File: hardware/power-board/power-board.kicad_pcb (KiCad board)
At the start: 2 copper layers, 197 x 65 mm, 26 parts, among them J1 SW_SPST, J2 Main Board, J3 DMX512 Out Jack, J4 DMX512, K1 SPST-NO, K2 SPST-NO, P1 IEC320-C14, P2 IEC320-C13, P3 IEC320-C13, U1 NUD3112DMT1G, U2 MAX3075E

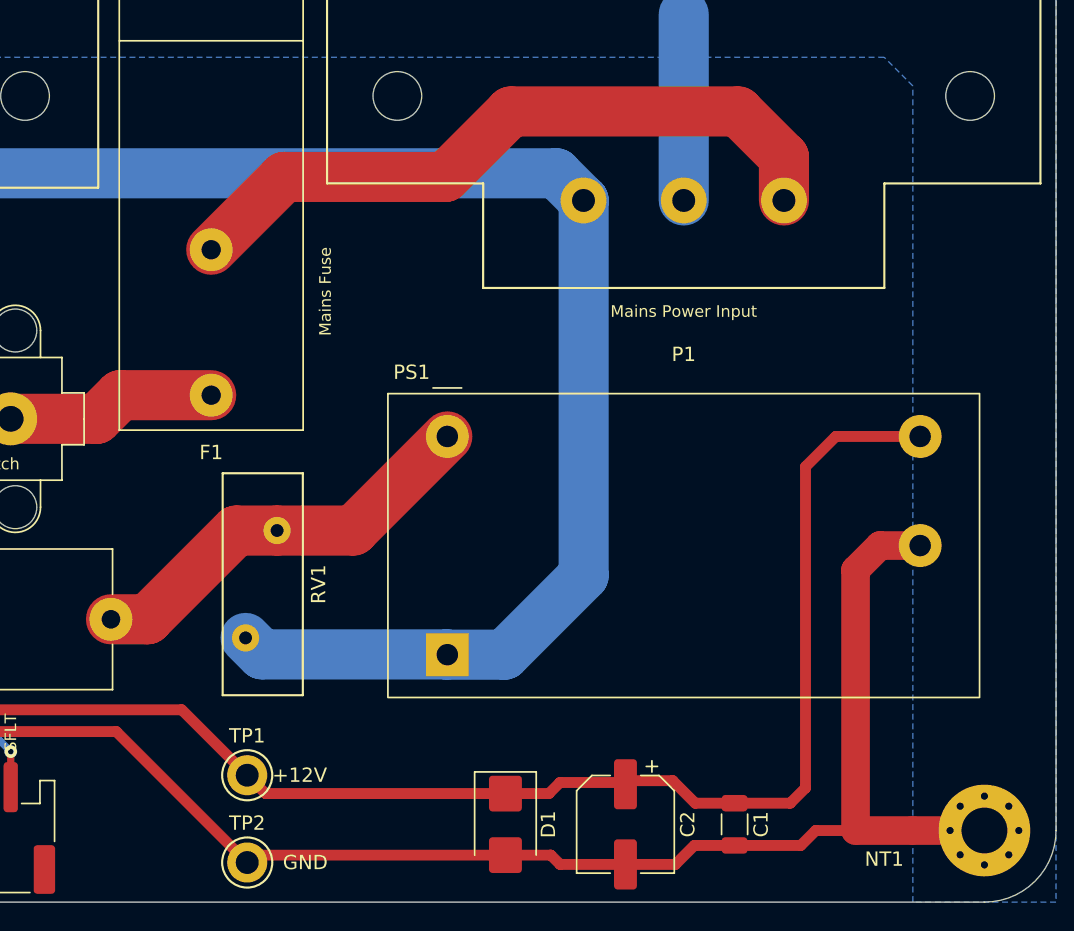
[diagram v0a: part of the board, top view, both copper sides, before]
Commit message: Swap AC/DC converter for IRM-10-12 and update output capacitor
A bit more comfortable with this option versus the other one, since it
likely has more protection and filtering.  Still may want to rearrange
and reroute some of the output components, which are a bit cramped at
the moment.
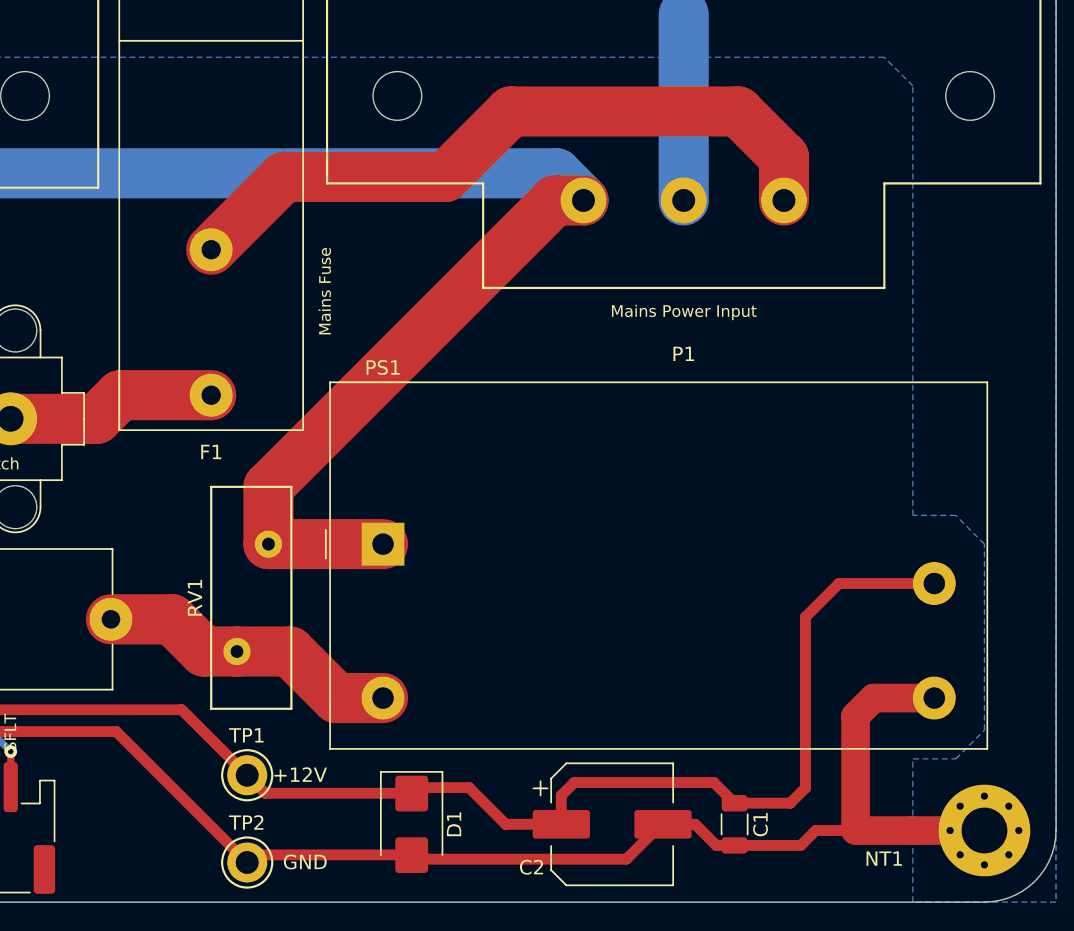
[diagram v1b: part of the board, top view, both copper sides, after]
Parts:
- C2: value 10uF -> 47uF; footprint Capacitor_SMD:CP_Elec_6.3x5.4 -> lib_fp:CP_Elec_8x10.2
- PS1: value CFM06S120-E -> IRM-10-12; footprint lib_fp:Converter_ACDC_Cincom_CFM06Sxxx-E -> Converter_ACDC:Converter_ACDC_MeanWell_IRM-10-xx_THT
- moved PS1 21.0 mm to (185.0, 80.0)
- moved RV1 6.74 mm to (177.0, 80.0), turned to -90 degrees
- moved D1 6.55 mm to (187.0, 99.6)
- moved C2 0.93 mm to (201.0, 99.6), turned to 0 degrees
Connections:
- PS1 pad 3: +12V -> GND
- PS1 pad 4: GND -> +12V
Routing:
- net NEUT: track 181.2 -> 170.9 mm
- net GND: track 117.0 -> 108.0 mm
- net /AC_L: track 28.8 -> 21.3 mm
- net +12V: track 191.6 -> 185.2 mm

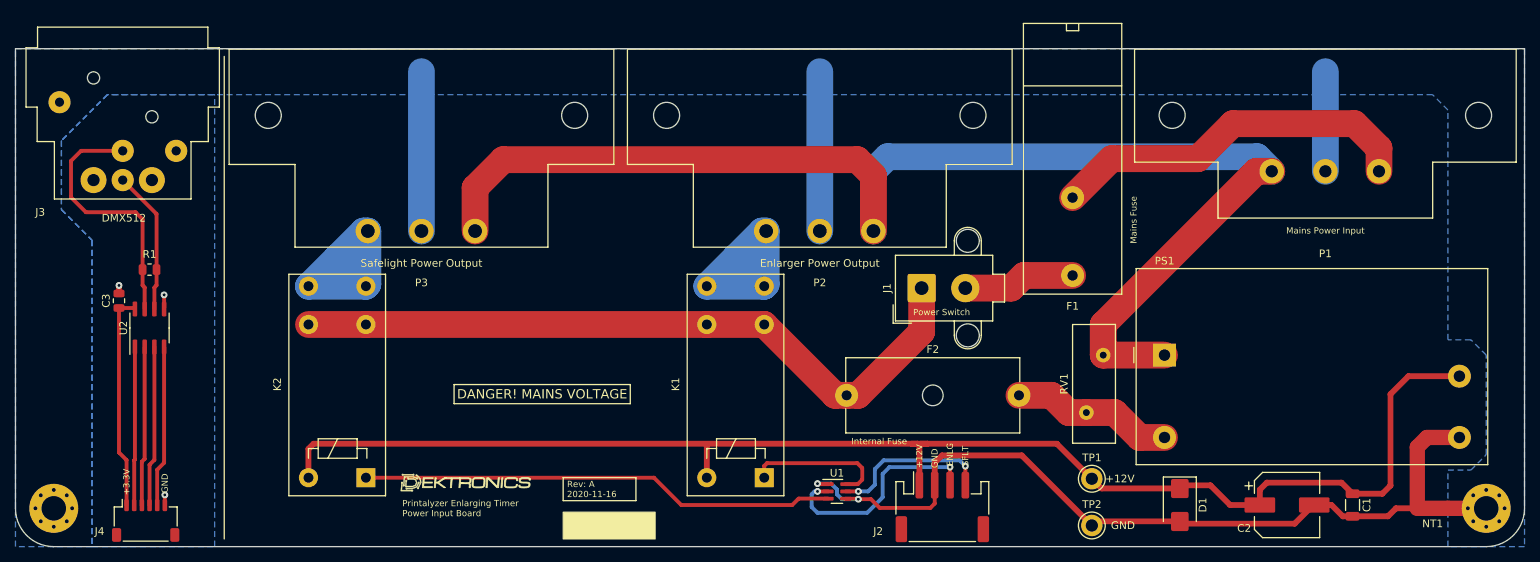
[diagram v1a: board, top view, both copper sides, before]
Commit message: Move components around for better clearance and update things
Moved the DC output filter components for better clearance
Moved one of the relays to make more space
Rerouted the relay control bits
Added a DC ground plane to make connections a bit better

Removed the net tie between DC ground and protective earth, as there's
still no good straight answer on how to do this. And they'll be
connected in other ways on the main board.
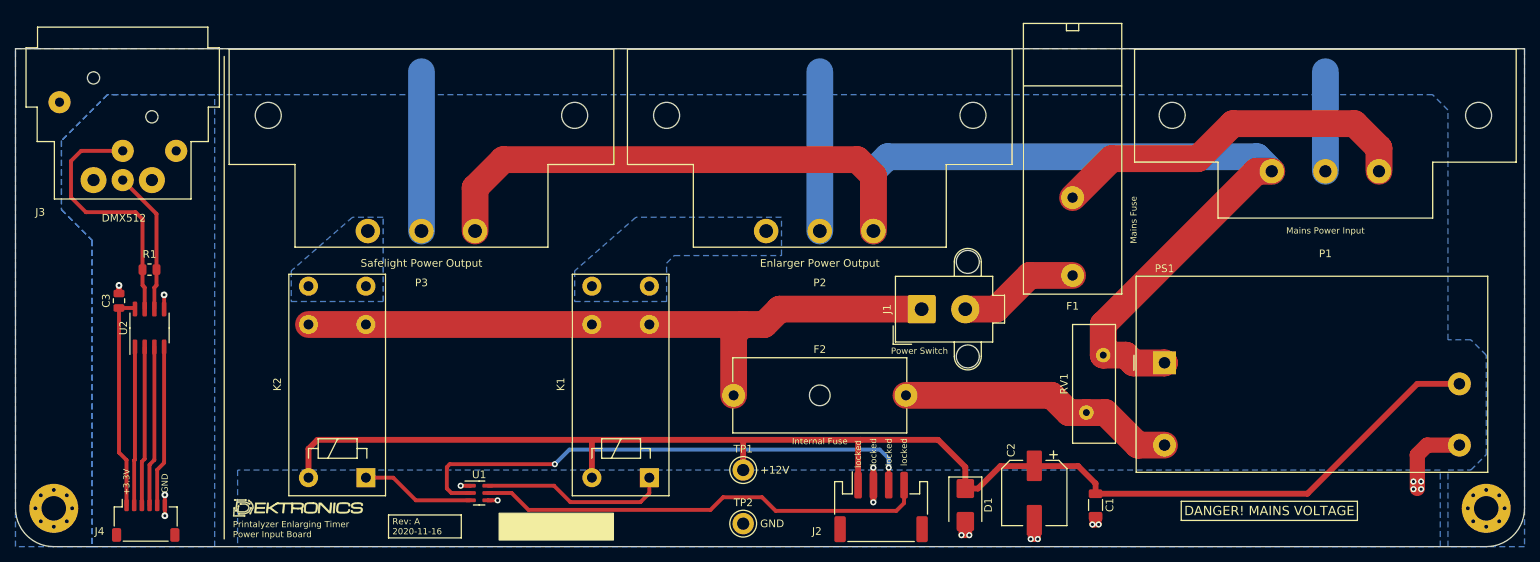
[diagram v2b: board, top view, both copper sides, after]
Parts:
- removed NT1: NetTie_2, NetTie:NetTie-2_SMD_Pad2.0mm
- moved U1 46.7 mm to (95.5, 98.0)
- moved TP1 45.5 mm to (130.0, 95.0)
- moved TP2 45.5 mm to (130.0, 102.0)
- moved C1 33.6 mm to (176.0, 99.6)
- moved C2 33.0 mm to (168.0, 98.0), turned to -90 degrees
- moved D1 28.0 mm to (159.0, 99.6)
- moved LOGO 22.1 mm to (72.1, 99.8)
- moved K1 15.0 mm to (110.2, 96.0)
- moved F2 14.8 mm to (128.8, 85.2)
- moved J2 8.00 mm to (148.0, 99.8)
- moved J1 2.75 mm to (153.3, 74.0)
- moved PS1 1.00 mm to (185.0, 81.0)
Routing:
- net GND: track 108.0 -> 37.8 mm, vias 2 -> 14
- net Net-(U1-DRAIN2): track 62.1 -> 14.9 mm
- net /RELAY_ENLARGER: track 28.9 -> 68.6 mm
- net /RELAY_SAFELIGHT: track 21.3 -> 59.4 mm, vias 2 -> 0
- net /ENLG_AC_L: track 30.9 -> 0.00 mm
- net /SFLT_AC_L: track 30.8 -> 0.00 mm
- net /AC_L: track 21.3 -> 36.4 mm
- net Net-(U1-DRAIN1): track 18.7 -> 24.5 mm
- net Earth: track 59.6 -> 54.6 mm
- net LINE: track 93.0 -> 90.6 mm
- net +12V: track 185.2 -> 183.2 mm
- net GND1: track 4.37 -> 5.74 mm, vias 3 -> 4
- net Net-(J1-B): track 14.7 -> 15.8 mm
- added copper zone on B.Cu, net /ENLG_AC_L
- added copper zone on B.Cu, net /SFLT_AC_L
- added copper zone on B.Cu, net GND
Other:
- board text added: "locked"
- board text removed: "ENLG"
- board text removed: "SFLT"

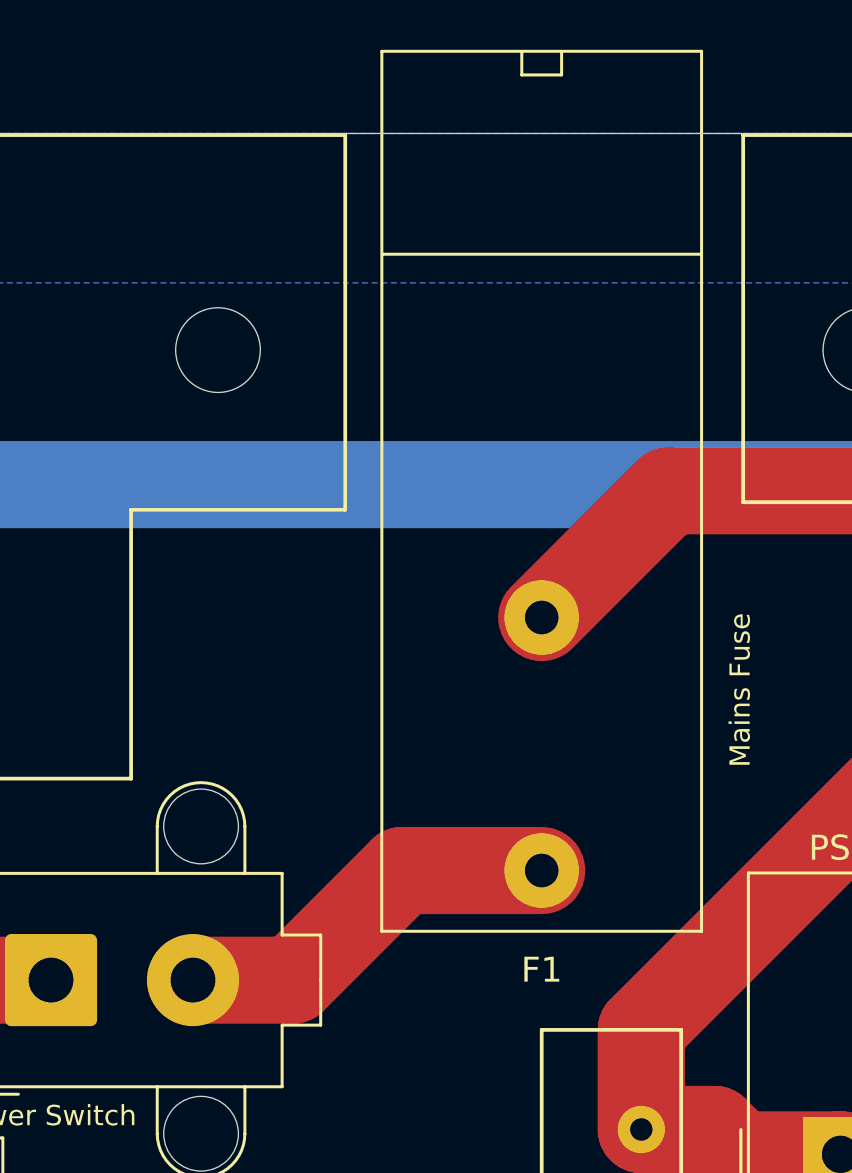
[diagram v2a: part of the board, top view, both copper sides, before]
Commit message: Changed fuse holder from Bulgin to Schurter
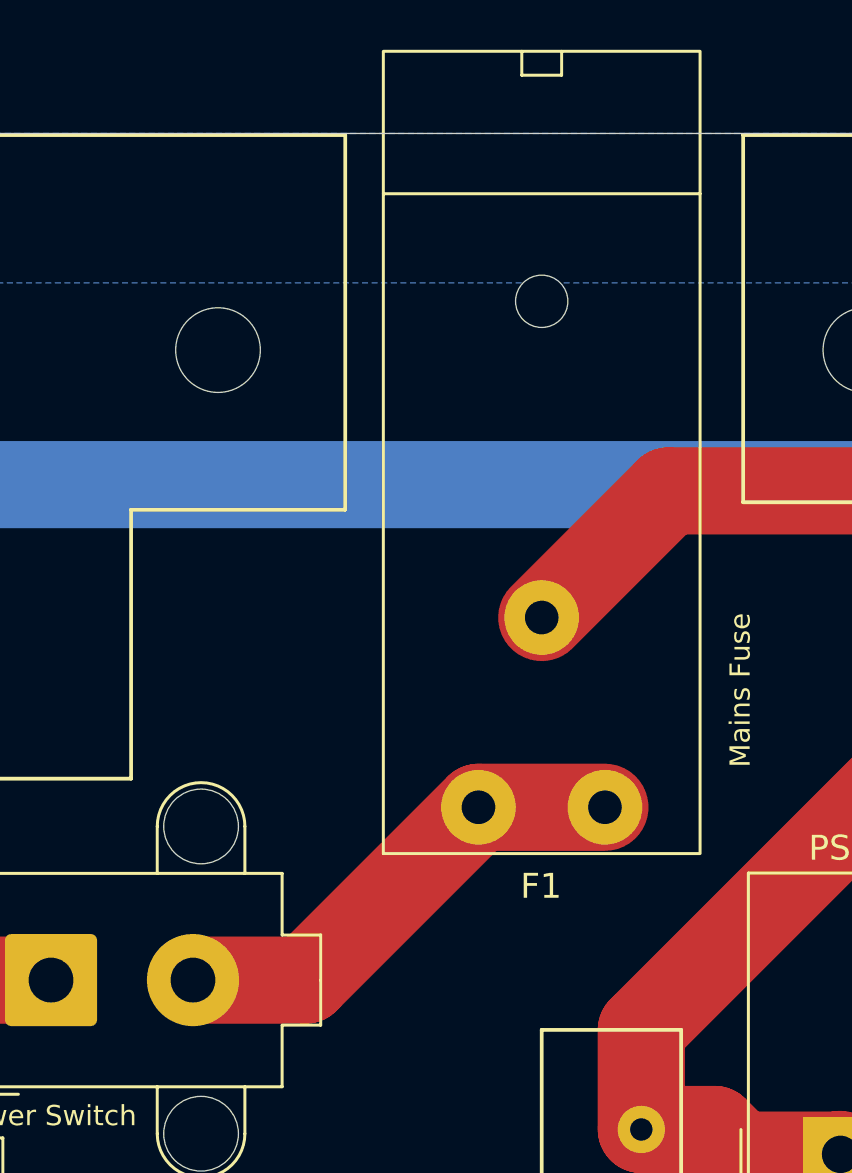
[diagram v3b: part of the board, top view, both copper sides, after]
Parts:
- F1: footprint Fuse:Fuseholder_Cylinder-5x20mm_Bulgin_FX0457_Horizontal_Closed -> lib_fp:Fuseholder_Cylinder-5x20mm_Schurter_FPG5_3101.0050_Horizontal_Closed
- moved F1 2.54 mm to (173.0, 67.1)
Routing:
- net Net-(J1-B): track 15.8 -> 19.4 mm
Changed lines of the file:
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@@
     )
   )
-  (footprint "Fuse:Fuseholder_Cylinder-5x20mm_Bulgin_FX0457_Horizontal_Closed" locked (layer "F.Cu")
-    (at 173 69.6 90)
-    (descr "Fuseholder, 5x20, closed, horizontal, Bulgin, FX0457, Sicherungshalter,")
-    (tags "Fuseholder 5x20 closed horizontal Bulgin FX0457 Sicherungshalter ")
-    (property "Description" "FUSE HLDR CARTRIDGE 250V 10A PCB")
-    (property "Manufacturer" "Bulgin")
-    (property "Manufacturer PN" "FX0457")
+  (footprint "lib_fp:Fuseholder_Cylinder-5x20mm_Schurter_FPG5_3101.0050_Horizontal_Closed" locked (layer "F.Cu")
+    (at 173 67.06 90)
+    (descr "Fuseholder, 5x20, closed, horizontal, Schurter, FPG5, 3101.0050")
+    (tags "Fuseholder 5x20 closed horizontal Schurter FPG5")
+    (property "Description" "FUSE HLDR CARTRIDGE 400V 16A PCB")
+    (property "Manufacturer" "Schurter")
+    (property "Manufacturer PN" "3101.0050")
     (property "Sheetfile" "power-board.kicad_sch")
     (property "Sheetname" "")
     (property "Supplier" "Digi-Key")
-    (property "Supplier PN" "708-1898-ND")
+    (property "Supplier PN" "486-1161-ND")
     (property "User Label" "Main Fuse")
     (property "ki_description" "Fuse")
     (property "ki_keywords" "fuse")
     (attr through_hole)
-    (fp_text reference "F1" (at -4 0 180) (layer "F.SilkS")
-        (effects (font (size 1 1) (thickness 0.15)))
-    )
-    (fp_text value "Fuse" (at 13.25 7.5 90) (layer "F.Fab")
-        (effects (font (size 1 1) (thickness 0.15)))
-    )
-    (fp_text user "${REFERENCE}" (at 13.25 5.5 90) (layer "F.Fab")
-        (effects (font (size 1 1) (thickness 0.15)))
-    )
-    (fp_line (start -2.44 -6.42) (end -2.44 6.42)
-      (stroke (width 0.12) (type solid)) (layer "F.SilkS"))
-    (fp_line (start -2.44 -6.42) (end 32.9 -6.42)
-      (stroke (width 0.12) (type solid)) (layer "F.SilkS"))
-    (fp_line (start 24.75 -6.4) (end 24.75 6.4)
-      (stroke (width 0.12) (type solid)) (layer "F.SilkS"))
-    (fp_line (start 31.95 -0.8) (end 31.95 0.8)
-      (stroke (width 0.12) (type solid)) (layer "F.SilkS"))
-    (fp_line (start 31.95 0.8) (end 32.85 0.8)
-      (stroke (width 0.12) (type solid)) (layer "F.SilkS"))
-    (fp_line (start 32.85 -0.8) (end 31.95 -0.8)
-      (stroke (width 0.12) (type solid)) (layer "F.SilkS"))
-    (fp_line (start 32.9 6.42) (end -2.44 6.42)
-      (stroke (width 0.12) (type solid)) (layer "F.SilkS"))
-    (fp_line (start 32.9 6.42) (end 32.9 -6.42)
-      (stroke (width 0.12) (type solid)) (layer "F.SilkS"))
-    (fp_line (start -2.57 -6.55) (end -2.57 6.55)
-      (stroke (width 0.05) (type solid)) (layer "F.CrtYd"))
-    (fp_line (start -2.57 -6.55) (end 33.03 -6.55)
-      (stroke (width 0.05) (type solid)) (layer "F.CrtYd"))
-    (fp_line (start 33.03 6.55) (end -2.57 6.55)
-      (stroke (width 0.05) (type solid)) (layer "F.CrtYd"))
-    (fp_line (start 33.03 6.55) (end 33.03 -6.55)
-      (stroke (width 0.05) (type solid)) (layer "F.CrtYd"))
-    (fp_line (start -2.32 6.3) (end -2.32 -6.3)
-      (stroke (width 0.1) (type solid)) (layer "F.Fab"))
-    (fp_line (start -2.32 6.3) (end 32.78 6.3)
-      (stroke (width 0.1) (type solid)) (layer "F.Fab"))
-    (fp_line (start 24.78 6.3) (end 24.78 -6.3)
-      (stroke (width 0.1) (type solid)) (layer "F.Fab"))
-    (fp_line (start 31.98 -0.8) (end 31.98 0.8)
-      (stroke (width 0.1) (type solid)) (layer "F.Fab"))
-    (fp_line (start 31.98 0.8) (end 32.78 0.8)
-      (stroke (width 0.1) (type solid)) (layer "F.Fab"))
-    (fp_line (start 32.78 -6.3) (end -2.32 -6.3)
-      (stroke (width 0.1) (type solid)) (layer "F.Fab"))
-    (fp_line (start 32.78 -0.8) (end 31.98 -0.8)
-      (stroke (width 0.1) (type solid)) (layer "F.Fab"))
-    (fp_line (start 32.78 6.3) (end 32.78 -6.3)
-      (stroke (width 0.1) (type solid)) (layer "F.Fab"))
-    (pad "1" thru_hole circle locked (at 0 0 90) (size 3 3) (drill 1.35) (layers "*.Cu" "*.Mask")
+    (fp_text reference "F1" (at -3.171 -0.026 180) (layer "F.SilkS")
+        (effects (font (size 1 1) (thickness 0.15)))
+    )
+    (fp_text value "Fuse" (at 13.25 7.8 90) (layer "F.Fab")
+        (effects (font (size 1 1) (thickness 0.15)))
+    )
+    (fp_text user "${REFERENCE}" (at 13.25 5 90) (layer "F.Fab")
+        (effects (font (size 1 1) (thickness 0.15)))
+    )
+    (fp_line (start 24.64 -6.36) (end 24.64 6.36)
+      (stroke (width 0.12) (type solid)) (layer "F.SilkS"))
+    (fp_line (start 29.4 -0.8) (end 29.4 0.8)
+      (stroke (width 0.12) (type solid)) (layer "F.SilkS"))
+    (fp_line (start 29.4 0.8) (end 30.36 0.8)
+      (stroke (width 0.12) (type solid)) (layer "F.SilkS"))
+    (fp_line (start 30.36 -0.8) (end 29.4 -0.8)
+      (stroke (width 0.12) (type solid)) (layer "F.SilkS"))
+    (fp_rect (start -1.86 -6.36) (end 30.36 6.36)
+      (stroke (width 0.12) (type default)) (fill none) (layer "F.SilkS"))
+    (fp_rect (start -2.25 -6.75) (end 30.75 6.75)
+      (stroke (width 0.05) (type default)) (fill none) (layer "F.CrtYd"))
+    (fp_line (start 24.75 6.25) (end 24.75 -6.25)
+      (stroke (width 0.1) (type solid)) (layer "F.Fab"))
+    (fp_line (start 29.4 -0.8) (end 29.4 0.8)
+      (stroke (width 0.1) (type solid)) (layer "F.Fab"))
+    (fp_line (start 29.4 0.8) (end 30.25 0.8)
+      (stroke (width 0.1) (type solid)) (layer "F.Fab"))
+    (fp_line (start 30.25 -0.8) (end 29.4 -0.8)
+      (stroke (width 0.1) (type solid)) (layer "F.Fab"))
+    (fp_rect (start -1.75 -6.25) (end 30.25 6.25)
+      (stroke (width 0.1) (type default)) (fill none) (layer "F.Fab"))
+    (pad "" np_thru_hole circle locked (at 20.32 0 90) (size 2.1 2.1) (drill 2.1) (layers "F&B.Cu" "*.Mask"))
+    (pad "1" thru_hole circle locked (at 0 -2.54 90) (size 3 3) (drill 1.35) (layers "*.Cu" "*.Mask")
       (net 18 "Net-(J1-B)") (pintype "passive"))
-    (pad "2" thru_hole circle locked (at 10.16 0 90) (size 3 3) (drill 1.35) (layers "*.Cu" "*.Mask")
+    (pad "1" thru_hole circle locked (at 0 2.54 90) (size 3 3) (drill 1.35) (layers "*.Cu" "*.Mask")
+      (net 18 "Net-(J1-B)") (pintype "passive"))
+    (pad "2" thru_hole circle locked (at 7.62 0 90) (size 3 3) (drill 1.35) (layers "*.Cu" "*.Mask")
       (net 24 "Net-(P1-AC_L)") (pintype "passive"))
-    (model "${KICAD6_3DMODEL_DIR}/Fuse.3dshapes/Fuseholder_Cylinder-5x20mm_Bulgin_FX0457_Horizontal_Closed.wrl"
-      (offset (xyz 0 0 0))
+    (model "${KIPRJMOD}/../library/3dmodels/lib_fp.3dshapes/Schurter_FPG5_3101_0050.step"
+      (offset (xyz 24.75 0 0))
       (scale (xyz 1 1 1))
-      (rotate (xyz 0 0 0))
+      (rotate (xyz -90 0 -90))
     )
   )
@@
   (via (at 54.5 98.25) (size 0.889) (drill 0.381) (layers "F.Cu" "B.Cu") (free) (net 17))
   (segment (start 54.229 72.009) (end 54.356 72.136) (width 0.508) (layer "B.Cu") (net 17))
-  (segment (start 173 69.6) (end 167.4 69.6) (width 3.500001) (layer "F.Cu") (net 18))
-  (segment (start 167.4 69.6) (end 163 74) (width 3.500001) (layer "F.Cu") (net 18))
-  (segment (start 163 74) (end 158.995 74) (width 3.500001) (layer "F.Cu") (net 18))
+  (segment (start 158.995 74) (end 163.52 74) (width 3.500001) (layer "F.Cu") (net 18))
+  (segment (start 170.46 67.06) (end 175.54 67.06) (width 3.500001) (layer "F.Cu") (net 18))
+  (segment (start 163.52 74) (end 170.46 67.06) (width 3.500001) (layer "F.Cu") (net 18))
   (segment (start 151.25 85.25) (end 170.25 85.25) (width 3.500001) (layer "F.Cu") (net 19))
   (segment (start 170.25 85.25) (end 172.5 87.5) (width 3.500001) (layer "F.Cu") (net 19))
